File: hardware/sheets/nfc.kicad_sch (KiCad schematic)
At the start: 13 parts, among them U1101 NT3H2111W0FHKH

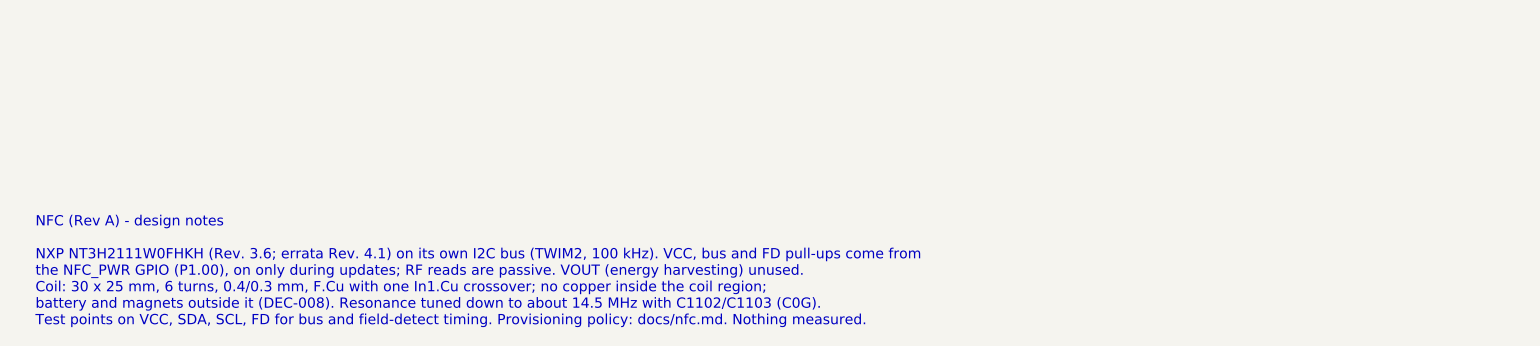
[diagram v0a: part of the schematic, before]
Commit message: hw: correct the E73 pad count and NFC TWIM note
The E73 footprint has 28 castellated pads (8 on the top edge, 10 per
side) and 15 inner pads; its description said 25 castellated pads,
which did not add up to the 43 pads it defines.

The nRF52840 provides only TWIM0 and TWIM1, so the NFC bus note no
longer names TWIM2: the NTAG bus uses TWIM1 and I2C1 uses TWIM0.
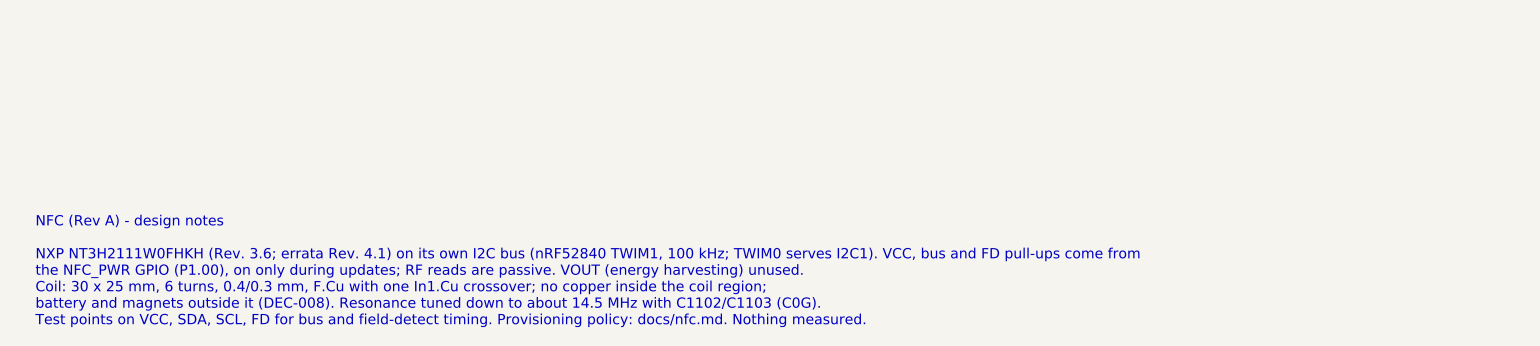
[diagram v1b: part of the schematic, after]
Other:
- note added: "NFC (Rev A) - design notes NXP NT3H2111W0FHKH (Rev. 3.6; errata Rev. 4.1) on its own I2C bus (nRF52840 TWIM1, 100 kHz; TWIM0 serves I2C1). VCC, bus and FD pull-ups come from the NFC_PWR GPIO (P1.00), on only during updates; RF reads are passive. VOUT (energy harvesting) unused. Coil: 30 x 25 mm, 6 turns, 0.4/0.3 mm, F.Cu with one In1.Cu crossover; no copper inside the coil region; battery and mag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"
- note removed: "NFC (Rev A) - design notes NXP NT3H2111W0FHKH (Rev. 3.6; errata Rev. 4.1) on its own I2C bus (TWIM2, 100 kHz). VCC, bus and FD pull-ups come from the NFC_PWR GPIO (P1.00), on only during updates; RF reads are passive. VOUT (energy harvesting) unused. Coil: 30 x 25 mm, 6 turns, 0.4/0.3 mm, F.Cu with one In1.Cu crossover; no copper inside the coil region; battery and magnets outside it (DEC-008). R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"
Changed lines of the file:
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@@
 		(comment 2 "Schematic frozen for layout after review 2026-10-07; not for fabrication until the release gate")
 	)
-	(text "NFC (Rev A) - design notes\n\nNXP NT3H2111W0FHKH (Rev. 3.6; errata Rev. 4.1) on its own I2C bus (TWIM2, 100 kHz). VCC, bus and FD pull-ups come from\nthe NFC_PWR GPIO (P1.00), on only during updates; RF reads are passive. VOUT (energy harvesting) unused.\nCoil: 30 x 25 mm, 6 turns, 0.4/0.3 mm, F.Cu with one In1.Cu crossover; no copper inside the coil region;\nbattery and magnets outside it (DEC-008). Resonance tuned down to about 14.5 MHz with C1102/C1103 (C0G).\nTest points on VCC, SDA, SCL, FD for bus and field-detect timing. Provisioning policy: docs/nfc.md. Nothing measured."
+	(text "NFC (Rev A) - design notes\n\nNXP NT3H2111W0FHKH (Rev. 3.6; errata Rev. 4.1) on its own I2C bus (nRF52840 TWIM1, 100 kHz; TWIM0 serves I2C1). VCC, bus and FD pull-ups come from\nthe NFC_PWR GPIO (P1.00), on only during updates; RF reads are passive. VOUT (energy harvesting) unused.\nCoil: 30 x 25 mm, 6 turns, 0.4/0.3 mm, F.Cu with one In1.Cu crossover; no copper inside the coil region;\nbattery and magnets outside it (DEC-008). Resonance tuned down to about 14.5 MHz with C1102/C1103 (C0G).\nTest points on VCC, SDA, SCL, FD for bus and field-detect timing. Provisioning policy: docs/nfc.md. Nothing measured."
 		(exclude_from_sim no)
 		(at 50.8 152.4 0)
